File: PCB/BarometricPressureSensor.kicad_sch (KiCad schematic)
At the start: 39 parts, among them J1 USB4105-GF-A, J2 54-00125, J3 Conn_01x02, J4 GTFP08441BEU, J5 2337019-1, J6 B3B-XH-A, J7 B6B-XH-A, U1 ESP32-S3-DEVKITC-1-N16R8V, U2 DPS368XTSA1, U3 BQ24074RGT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

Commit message: Add files via upload
Updated the switch we are using for the PCB. Will need to order these switches on our own.
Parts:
- removed J3: Conn_01x02, B2B_XH_A:JST_B2B-XH-A, symbol Connector_Generic:Conn_01x02
- removed J6: B3B-XH-A, B3B_XH_A:JST_B3B-XH-A, symbol B3B-XH-A:B3B-XH-A
- removed J7: B6B-XH-A, B6B_XH_A:JST_B6B-XH-A, symbol B6B-XH-A:B6B-XH-A
- added J10: B2B-PH-K-S, B2B_PH_K_S:JST_B2B-PH-K-S, symbol B2B-PH-K-S:B2B-PH-K-S
- added J8: B6B-PH-K-S, B6B_PH_K_S:JST_B6B-PH-K-S, symbol B6B-PH-K-S:B6B-PH-K-S
- added J9: B3B-PH-K-S, B3B_PH_K_S:JST_B3B-PH-K-S, symbol B3B-PH-K-S:B3B-PH-K-S
- added S1: EG1213, EG1213:SW_EG1213, symbol EG1213:EG1213
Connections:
- net +3V3: now also J8.1
- net +BATT: now also J10.1, S1.1, S1.2
- net CS2: now also J8.2
- net DPSCLK: now also J8.5
- net DPSMISO: now also J8.4
- net DPSMOSI: now also J8.3
- net GND: now also J10.2, J8.6
- net OLEDBUT: now also J9.3
- net OLEDSCL: now also J9.2
- net OLEDSDA: now also J9.1
- no-connect marks 0 -> 1
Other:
- moved on the sheet: J4, R10, R11, R7, R8, R9

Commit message: Add files via upload
Updated PPS and SD Schematic
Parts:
- U2: DESCRIPTION Package dimensions: 8-pin LGA, 2.0 x 2.5 x 1.1 mm3 | Operat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 -> (none)
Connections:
- net +3V3: now also J4.4 (VDD); no longer J4.6 (VSS)
- net GND: now also J4.6 (VSS)
- net PPS: now reaches U1.J3_9 (MTCK/GPIO39)
- net PPS: now also U6.13 (1PPS)
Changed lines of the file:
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@@
 (kicad_sch
-	(version 20250114)
+	(version 20260306)
 	(generator "eeschema")
-	(generator_version "9.0")
+	(generator_version "10.0")
 	(paper "A4")

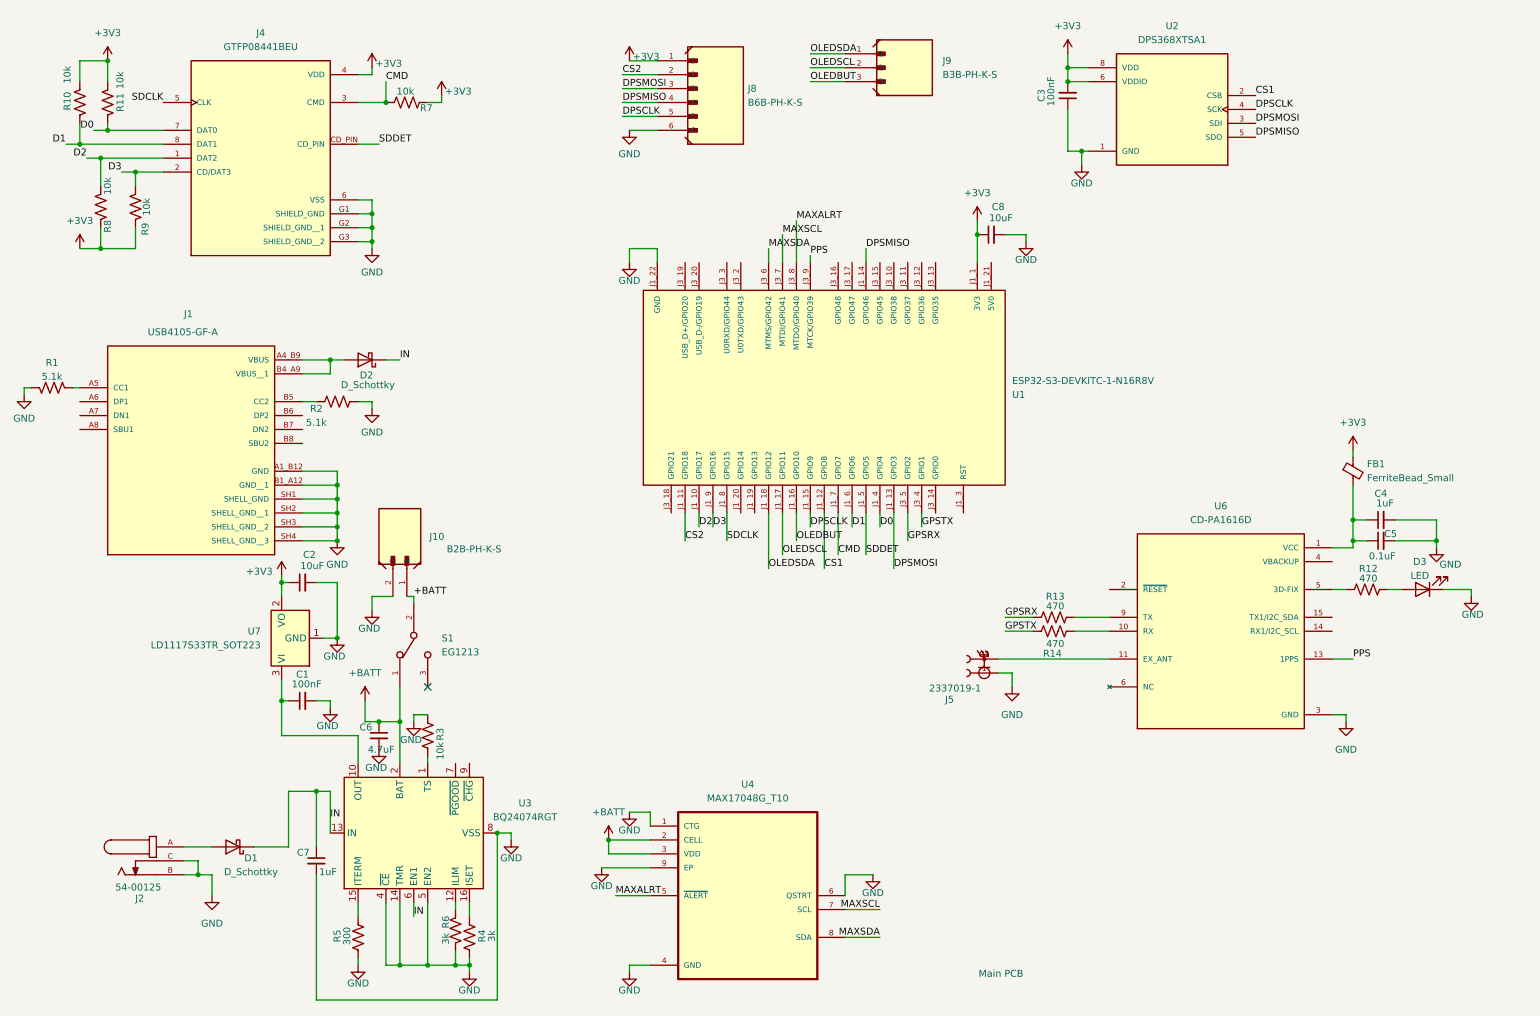
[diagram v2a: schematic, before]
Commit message: Annotated main board schematic, corrected switch short on main PCB
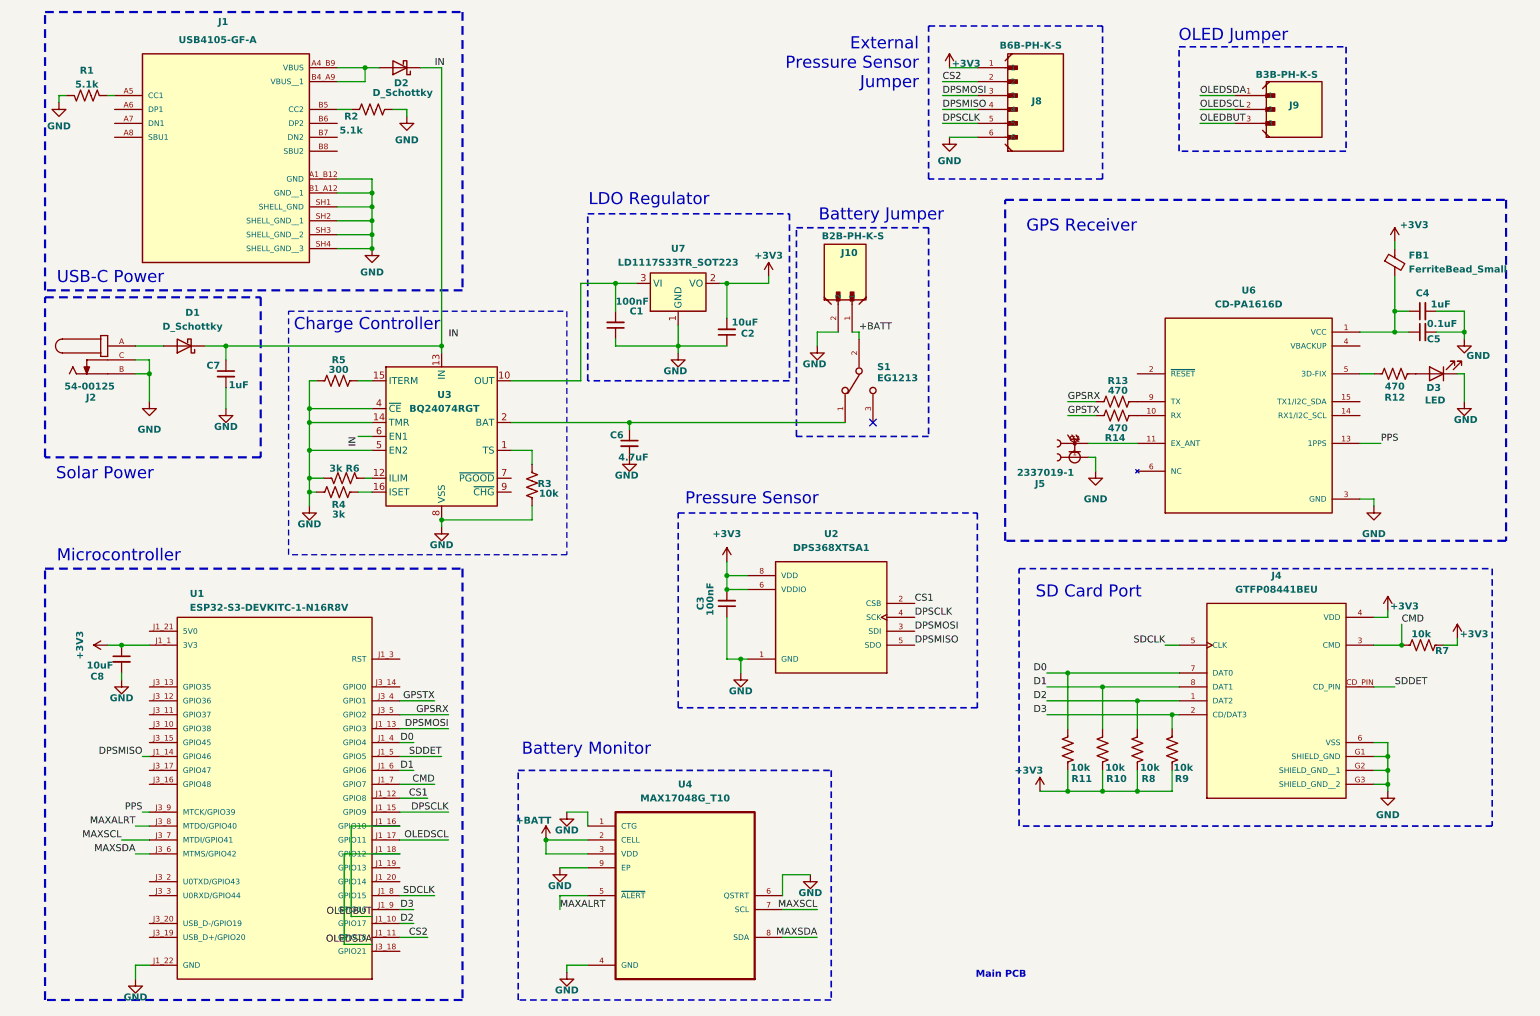
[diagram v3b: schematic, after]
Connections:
- net +3V3: now also C2.2, R10.1, R11.1; no longer C2.1, R10.2, R11.2
- net +BATT: no longer C6.1, S1.1, U3.2 (BAT), U3.3 (BAT)
- net D0: now also R11.2; no longer R11.1
- net D1: now also R10.2; no longer R10.1
- net GND: now also C1.1, C2.1, R3.1; no longer C1.2, C2.2, R3.2
- net at U3.10 (OUT), U3.11 (OUT), U7.3 (VI): now also C1.2; no longer C1.1
- net at U3.1 (TS): now also R3.2; no longer R3.1
- new net: C6.1, S1.1, U3.2 (BAT), U3.3 (BAT)
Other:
- note added: "Battery Jumper"
- note added: "Battery Monitor"
- note added: "External Pressure Sensor Jumper"
- note added: "GPS Receiver"
- note added: "LDO Regulator"
- note added: "Microcontroller"
- note added: "OLED Jumper"
- note added: "Pressure Sensor"
- note added: "SD Card Port"
- note added: "Solar Power"
- note added: "USB-C Power"
- moved on the sheet: C1, C2, C3, C4, C5, C6, C7, C8, D1, D2, D3, FB1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
